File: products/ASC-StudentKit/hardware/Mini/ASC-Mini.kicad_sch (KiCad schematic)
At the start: 92 parts, among them J1 12V IN, J10 OUT2, J2 USB-C, J3 PROG, J4 S1, J5 S2, J6 S3, J7 S4, J8 I2C-1 (Grove), J9 OUT1, K1 SRD-05VDC-SL-C, K2 SRD-05VDC-SL-C, Q1 AO3400A, Q2 AO3400A, Q3 AO3400A, SW1 RESET, SW2 PAIR / BOOT, U1 ESP32-S3-MINI-1-N8, U2 TPS54202DDC, U3 USBLC6-2SC6, U4 AP7361C-33E, U5 DS3231MZ+

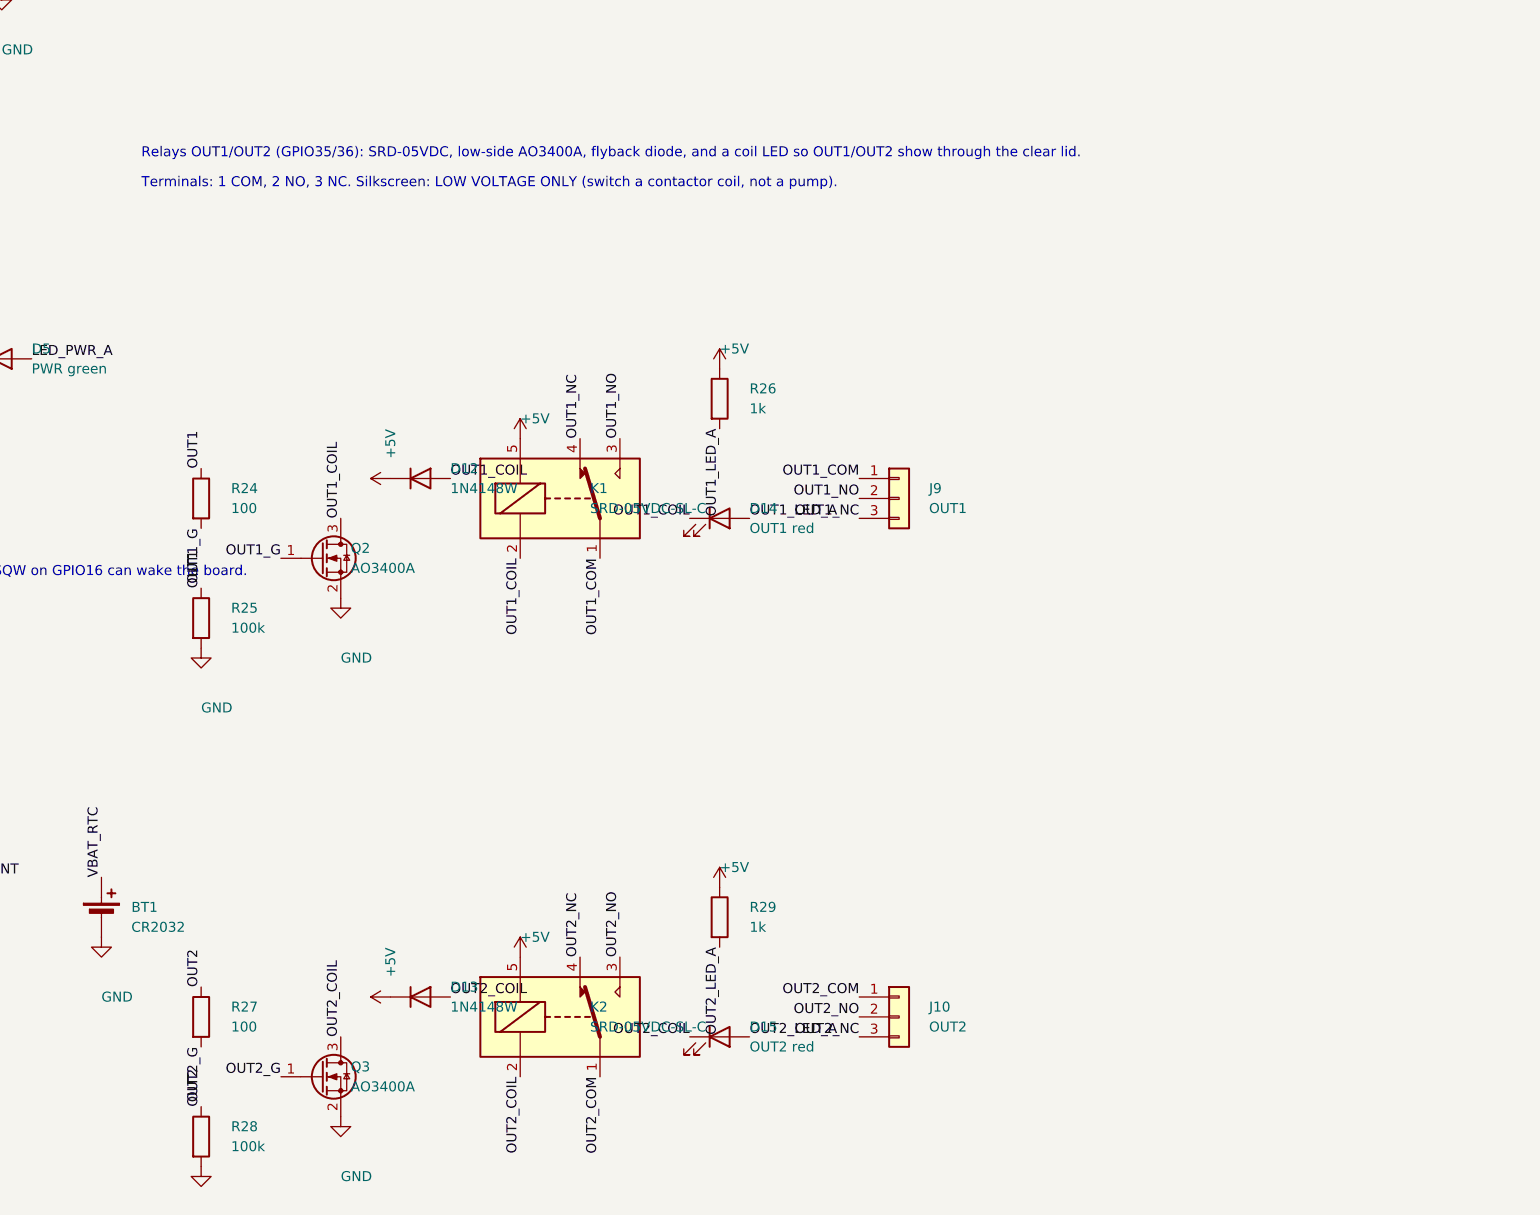
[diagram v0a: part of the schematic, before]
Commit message: Mini: Hongfa HF46F relays; drop the OLED from the kits
Relays: the slim HF46F (1 Form A, 20.5 x 7.2 mm) replaces the SRD, so the
OUT terminals are 2-way (COM, NO). KiCad has no HF46F, so the project gets
its own libraries: ASC.pretty with a footprint drawn from the Hongfa
datasheet's PCB layout, and ASC.kicad_sym with a symbol derived from
Omron's G5Q-1A and renumbered to the HF46F pads.

24 V maximum input is agreed, which the TPS54202 and SMAJ26A suit.

No OLED in the kits: the phone app is the screen. The OLED block is gone
from the studio's library, the Wokwi simulation, the test plan, the
enclosure checks and the firmware (driver, display code and the SSD1306
library). Specs and architecture updated.

Co-Authored-By: Claude Opus 5.5 <noreply@anthropic.com>
Claude-Session: https://claude.ai/code/session_0137TCDSR58nWZn1byy7MgSb
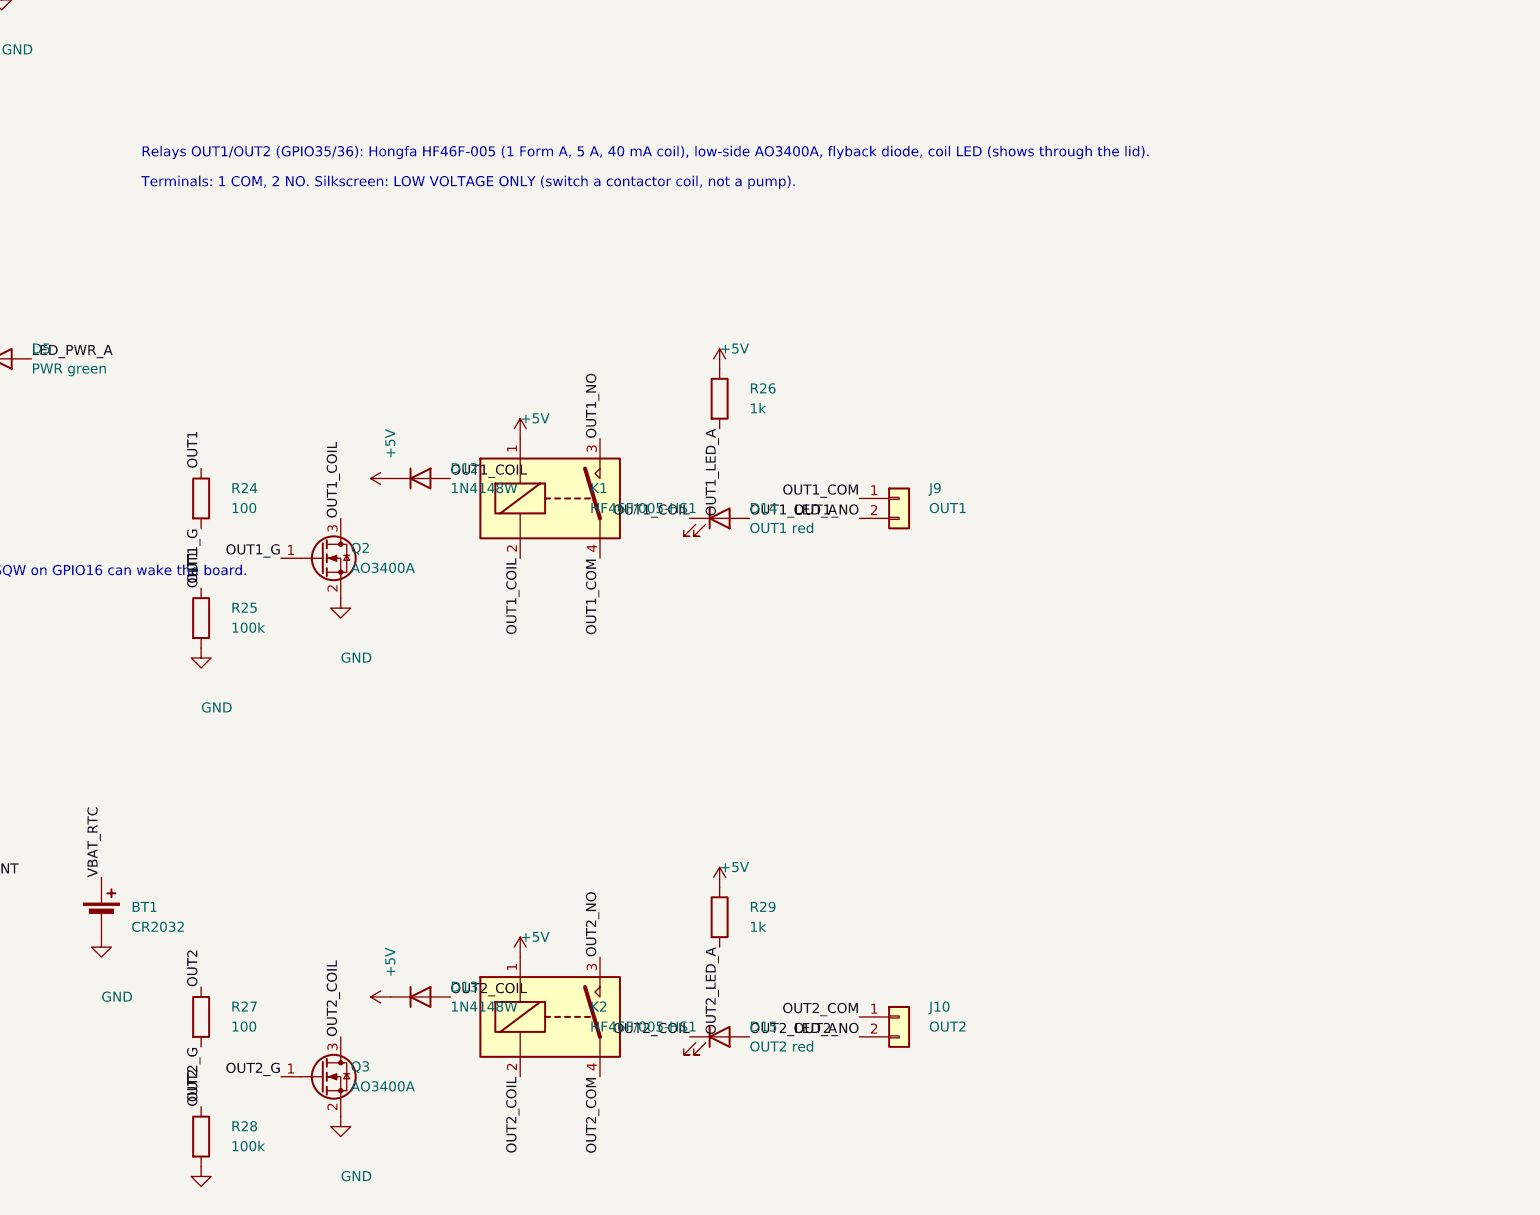
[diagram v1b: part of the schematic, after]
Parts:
- removed J10: OUT2, Connector_Phoenix_MSTB:PhoenixContact_MSTBA_2,5_3-G-5,08_1x03_P5.08mm_Horizontal, symbol Connector_Generic:Conn_01x03
- removed J9: OUT1, Connector_Phoenix_MSTB:PhoenixContact_MSTBA_2,5_3-G-5,08_1x03_P5.08mm_Horizontal, symbol Connector_Generic:Conn_01x03
- removed K1, K2: SRD-05VDC-SL-C, Relay_THT:Relay_SPDT_SANYOU_SRD_Series_Form_C, symbol Relay:SANYOU_SRD_Form_C
- added J10: OUT2, Connector_Phoenix_MSTB:PhoenixContact_MSTBA_2,5_2-G-5,08_1x02_P5.08mm_Horizontal, symbol Connector_Generic:Conn_01x02
- added J9: OUT1, Connector_Phoenix_MSTB:PhoenixContact_MSTBA_2,5_2-G-5,08_1x02_P5.08mm_Horizontal, symbol Connector_Generic:Conn_01x02
- added K1, K2: HF46F/005-HS1, ASC:Relay_SPST_Hongfa_HF46F, symbol ASC:HF46F
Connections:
- net +5V: now also K1.1, K2.1
- net OUT1_COIL: now also K1.2
- net OUT1_COM: now also J9.1 (Pin_1), K1.4
- net OUT1_NO: now also J9.2 (Pin_2), K1.3
- net OUT2_COIL: now also K2.2
- net OUT2_COM: now also J10.1 (Pin_1), K2.4
- net OUT2_NO: now also J10.2 (Pin_2), K2.3
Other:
- note added: "Relays OUT1/OUT2 (GPIO35/36): Hongfa HF46F-005 (1 Form A, 5 A, 40 mA coil), low-side AO3400A, flyback diode, coil LED (shows through the lid)."
- note added: "Terminals: 1 COM, 2 NO. Silkscreen: LOW VOLTAGE ONLY (switch a contactor coil, not a pump)."
- note removed: "Relays OUT1/OUT2 (GPIO35/36): SRD-05VDC, low-side AO3400A, flyback diode, and a coil LED so OUT1/OUT2 show through the clear lid."
- note removed: "Terminals: 1 COM, 2 NO, 3 NC. Silkscreen: LOW VOLTAGE ONLY (switch a contactor coil, not a pump)."

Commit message: Mini PCB: outline, holes and placement, generated by tools/gen_pcb.py
A plain-python board generator (no pcbnew needed): 97.4 x 47 mm with R15
top corners and 3 x M3 on the box's upper bosses. Terminals J1 (12 V IN),
J9/J10 (OUT1/OUT2) on the bottom edge facing the glands; S1-S4 and I2C-1
in the row above; the ESP32-S3 module right of the centre boss with its
antenna on the top edge and a keep-out rule area; HF46F relays beside it;
USB-C on the left edge; RESET/PAIR on the top edge; the buzzer in the
rounded corner. Small parts are packed next to the pins they serve.
Every courtyard is checked against the outline, the screw bosses, the
antenna keep-out and the other parts. GND zones on both layers; port,
LED and LOW VOLTAGE ONLY labels on the silkscreen.

The RTC cell holder changes to the flat SMD Keystone 3034 on the back:
the MYOUNG BS-07 is a vertical through-hole part.

tools/check_board.py checks pads against the edge and screw heads and
that every net is on the board. Not routed yet.

Co-Authored-By: Claude Opus 5.5 <noreply@anthropic.com>
Claude-Session: https://claude.ai/code/session_0137TCDSR58nWZn1byy7MgSb
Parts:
- BT1: footprint Battery:BatteryHolder_MYOUNG_BS-07-A1BJ001_CR2032 -> Battery:BatteryHolder_Keystone_3034_1x20mm

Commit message: Mini PCB: GND left to the pours, routing fixes
route.py leaves GND out of the autorouter: after import, each front SMD
GND pad gets a short track to its own via into the back pour, and a 4 mm
grid of stitching vias ties the two pours together. Every via and track
is checked for clearance against all other copper, the board edge, the
screw bosses and the antenna keep-out. Second run: 2 nets left open
(from 19). Clearance rule 0.19 mm (the USB-C footprint's own pad gaps
are exactly 0.2 mm).

Placement: R5 (VIN sense top) sits by the buck so VIN stays local; the
buzzer gate parts sit on Q1's gate; LED labels go under their LEDs. U3's
VBUS reference pin moves to VBUS (before the fuse).

Board in this commit is unrouted; the next run's result follows.

Co-Authored-By: Claude Opus 5.5 <noreply@anthropic.com>
Claude-Session: https://claude.ai/code/session_0137TCDSR58nWZn1byy7MgSb
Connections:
- net VBUS: now also U3.5 (VBUS)
- net VBUS_F: no longer U3.5 (VBUS)

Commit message: Mini: 0402 passives, test header as pogo pads under the module
Staying on two layers frees routing room: the small resistors and
capacitors go from 0603 to 0402, and J3 (the tester's 8 pins) becomes an
SMD pad row on the back under the ESP32 module, not fitted (DNP), next
to the pins it serves instead of across the board. route.py gains
ROUTE_STAGE=all (GND routed with everything else). Board unrouted in
this commit; routing variants are running.

Co-Authored-By: Claude Opus 5.5 <noreply@anthropic.com>
Claude-Session: https://claude.ai/code/session_0137TCDSR58nWZn1byy7MgSb
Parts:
- C11, C13, C14, C15, C3, C4, C7, C9: footprint Capacitor_SMD:C_0603_1608Metric -> Capacitor_SMD:C_0402_1005Metric
- J3: value PROG -> PROG (pogo pads); footprint Connector_PinHeader_1.27mm:PinHeader_1x08_P1.27mm_Vertical -> Connector_PinHeader_1.27mm:PinHeader_1x08_P1.27mm_Vertical_SMD_Pin1Left; Side (none) -> back; now not fitted; now left out of the parts list
- R1, R10, R11, R12, R13, R14, R15, R16, R17, R18, R19, R2, R20, R21, R22, R23, R24, R25, R26, R27, R28, R29, R3, R4, R5, R6, R7, R8, R9: footprint Resistor_SMD:R_0603_1608Metric -> Resistor_SMD:R_0402_1005Metric
